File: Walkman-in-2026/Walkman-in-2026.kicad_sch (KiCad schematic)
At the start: 11 parts, among them J1 AudioJack3, J2 Micro_SD_Card, SW1 SW_Push, SW2 SW_Push, SW3 SW_Push, SW4 SW_SPST, U1 XIAO-ESP32-S3-DIP, U2 HS1602A-B, U3 PCM5102, U4 PCF8574P

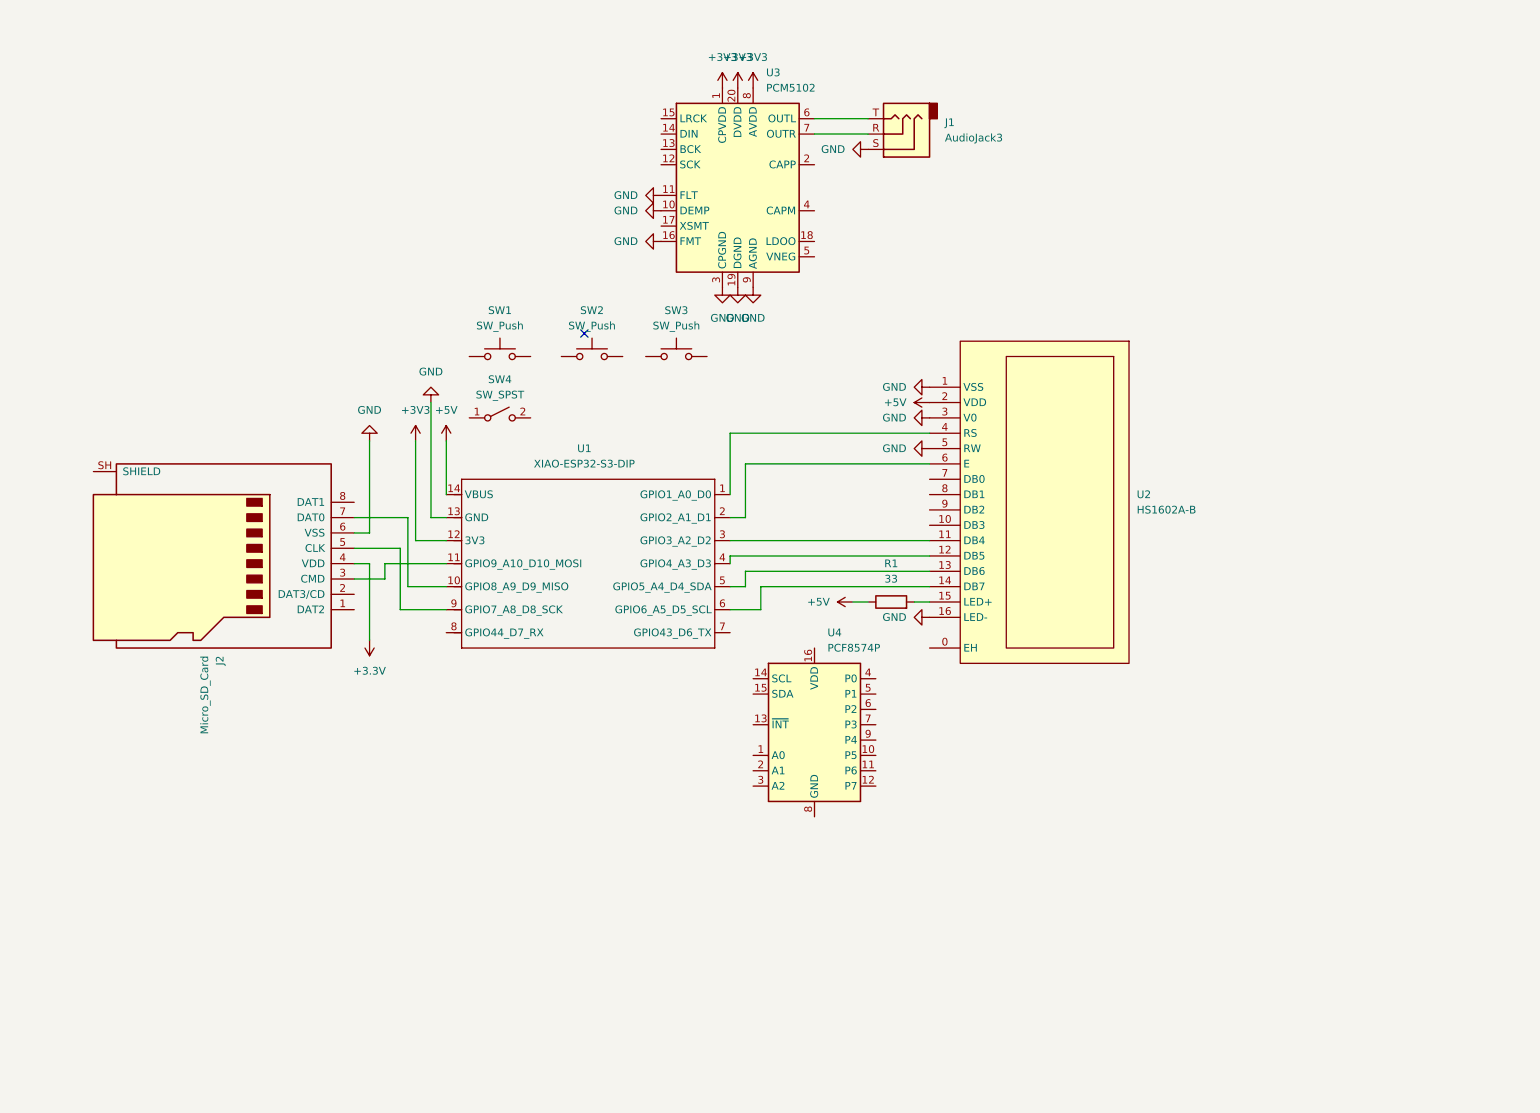
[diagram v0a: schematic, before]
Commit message: April 24 Session (Rerouting, Audio, Micro SD Card, and Setting Up Capacitors)
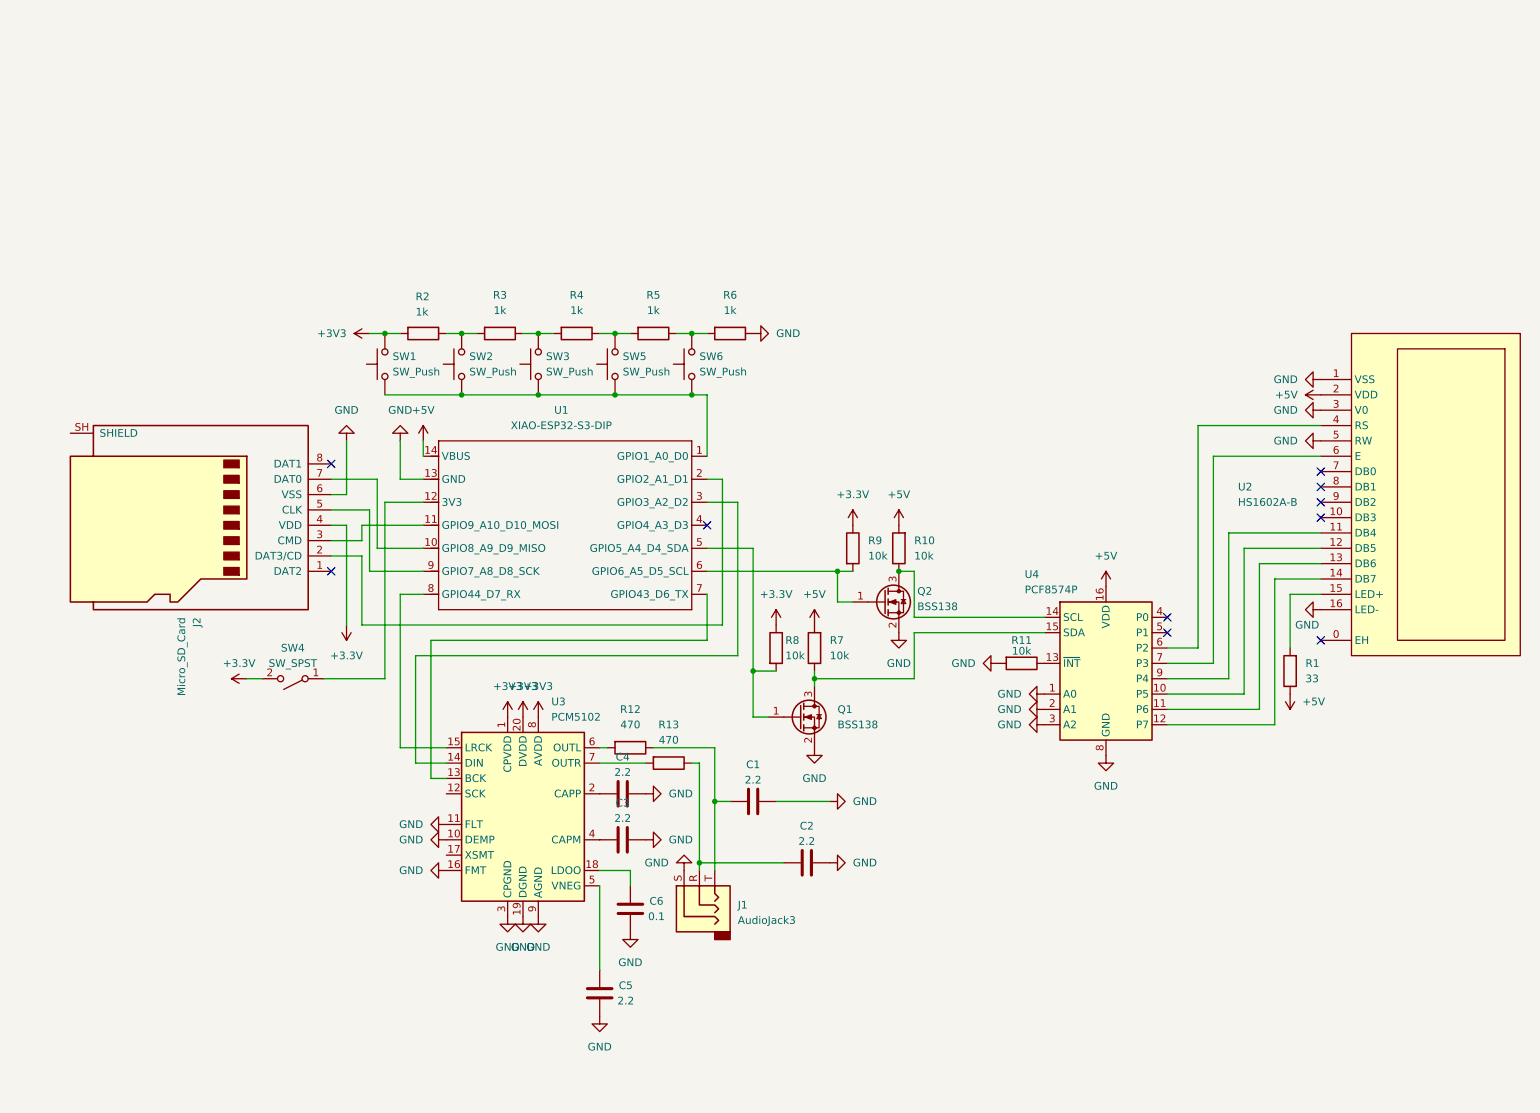
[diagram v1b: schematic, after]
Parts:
- added C1, C2, C3, C4, C5: 2.2, symbol Device:C
- added C6: 0.1, symbol Device:C
- added Q1, Q2: BSS138, Package_TO_SOT_SMD:SOT-23, symbol Transistor_FET:BSS138
- added R10, R11, R7, R8, R9: 10k, symbol Device:R
- added R12, R13: 470, symbol Device:R
- added R2, R3, R4, R5, R6: 1k, symbol Device:R
- added SW5, SW6: SW_Push, symbol Switch:SW_Push
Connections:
- net +3.3V: now also SW4.2 (B), R8.1, R9.1
- net +3V3: now also SW1.2, R2.2; no longer U1.12 (3V3)
- net +5V: now also U4.16 (VDD), R10.2, R7.2
- net GND: now also U4.1 (A0), U4.2 (A1), U4.3 (A2), U4.8 (GND), C1.2, C2.2, C3.2, C4.2, C5.2, C6.2, Q1.2 (S), Q2.2 (S), R11.2, R6.1
- net at U4.10 (P5): now also U2.12 (DB5)
- net at U4.11 (P6): now also U2.13 (DB6)
- net at U4.12 (P7): now also U2.14 (DB7)
- net at U4.13 (~{INT}): now also R11.1
- net at U4.14 (SCL): now also Q2.3 (D), R10.1
- net at U4.15 (SDA): now also Q1.3 (D), R7.1
- net at U4.6 (P2): now also U2.4 (RS)
- net at U4.7 (P3): now also U2.6 (E)
- net at U4.9 (P4): now also U2.11 (DB4)
- net at U3.13 (BCK): now also U1.7 (GPIO43_D6_TX)
- net at U3.14 (DIN): now also U1.3 (GPIO3_A2_D2)
- net at U3.15 (LRCK): now also U1.8 (GPIO44_D7_RX)
- net at U3.18 (LDOO): now also C6.1
- net at U3.2 (CAPP): now also C4.1
- net at U3.4 (CAPM): now also C3.1
- net at U3.5 (VNEG): now also C5.1
- net at U3.6 (OUTL): now also R12.2; no longer J1.T
- net at J1.R: now also C2.1, R13.1; no longer U3.7 (OUTR)
- net at J2.2 (DAT3/CD): now also U1.2 (GPIO2_A1_D1)
- net at SW4.1 (A): now also U1.12 (3V3)
- net at U1.1 (GPIO1_A0_D0): now also SW1.1, SW2.1, SW3.1, SW5.1, SW6.1; no longer U2.4 (RS)
- net at U1.4 (GPIO4_A3_D3): no longer U2.12 (DB5)
- net at U1.5 (GPIO5_A4_D4_SDA): now also Q1.1 (G), R8.2; no longer U2.13 (DB6)
- net at U1.6 (GPIO6_A5_D5_SCL): now also Q2.1 (G), R9.2; no longer U2.14 (DB7)
- net at SW3.2: now also R3.1, R4.2
- net at SW2.2: now also R2.1, R3.2
- new net: R5.1, R6.2, SW6.2
- new net: R4.1, R5.2, SW5.2
- new net: R13.2, U3.7 (OUTR)
- new net: C1.1, J1.T, R12.1
- no-connect marks 1 -> 10
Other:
- moved on the sheet: J1, J2, R1, SW1, SW2, SW3, SW4, U1, U2, U3, U4

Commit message: jazz fest working
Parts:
- added C10, C9: C, symbol Device:C
- added C7, C8: 0.1, symbol Device:C
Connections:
- net +3V3: now also U3.17 (XSMT), C10.1, C7.2, C8.2, C9.2
- net GND: now also U3.12 (SCK), C10.2, C7.1, C8.1, C9.1
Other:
- moved on the sheet: C1, C2, C3, C4, C5, C6, J1, R12, R13, U3

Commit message: moving on to the pcb editor
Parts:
- removed C4: 2.2, symbol Device:C
- C1, C2, C6, C7, C8: footprint (none) -> Capacitor_THT:C_Disc_D3.0mm_W1.6mm_P2.50mm
- C10: value C -> 10; footprint (none) -> Capacitor_THT:C_Radial_D5.0mm_H5.0mm_P2.00mm
- C3, C5: footprint (none) -> Capacitor_THT:C_Radial_D5.0mm_H5.0mm_P2.00mm
- C9: value C -> 0.1; footprint (none) -> Capacitor_THT:C_Radial_D5.0mm_H5.0mm_P2.00mm
- J1: footprint (none) -> Connector_Audio:Jack_3.5mm_CUI_SJ1-3513N_Horizontal
- J2: footprint (none) -> Connector_Card:microSD_HC_Molex_47219-2001
- R1, R10, R11, R12, R13, R2, R3, R4, R5, R6, R7, R8, R9: footprint (none) -> Resistor_THT:R_Axial_DIN0207_L6.3mm_D2.5mm_P7.62mm_Horizontal
- SW1, SW2, SW3, SW5, SW6: footprint (none) -> Button_Switch_THT:SW_PUSH_6mm
- SW4: footprint (none) -> Button_Switch_THT:SW_SPST_Omron_B3F-315x_Angled
- U1: footprint Seeed_Studio_XIAO_Series:XIAO-ESP32-S3-DIP -> More_XIAO_Series_Footprints:XIAO-ESP32-S3-DIP
- U2: footprint easyeda2kicad:LCD1602 -> EasyEDALibrary:LCD1602
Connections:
- net GND: now also C1.1, C2.1; no longer C1.2, C2.2, C3.2
- net at J1.R, R13.1: now also C2.2; no longer C2.1
- net at U3.2 (CAPP): now also C3.1
- net at U3.4 (CAPM): now also C3.2; no longer C3.1
- net at J1.T, R12.1: now also C1.2; no longer C1.1
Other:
- moved on the sheet: C1, C2, C3, C5, C6, C7, C8, J1, J2, Q1, Q2, R1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

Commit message: adding a fking stupid battery
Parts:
- added BT1: Battery, symbol Device:Battery
- added J3: Conn_01x02_Socket, Connector_Molex:Molex_KK-254_AE-6410-02A_1x02_P2.54mm_Vertical, symbol Connector:Conn_01x02_Socket
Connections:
- net +3.3V: now also U1.12 (3V3); no longer SW4.2 (B)
- net +5V: no longer U1.14 (VBUS)
- net GND: now also J3.2 (Pin_2)
- net at SW4.1 (A): now also U1.14 (VBUS); no longer U1.12 (3V3)
- new net: BT1.2 (-), SW4.2 (B)
- new net: BT1.1 (+), J3.1 (Pin_1)
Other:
- moved on the sheet: SW4

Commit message: larp
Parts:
- removed BT1: Battery, symbol Device:Battery
- removed C1, C2: 2.2, Capacitor_THT:C_Disc_D3.0mm_W1.6mm_P2.50mm, symbol Device:C
- removed C10: 10, Capacitor_THT:C_Radial_D5.0mm_H5.0mm_P2.00mm, symbol Device:C
- removed C3, C5: 2.2, Capacitor_THT:C_Radial_D5.0mm_H5.0mm_P2.00mm, symbol Device:C
- removed C6, C7, C8: 0.1, Capacitor_THT:C_Disc_D3.0mm_W1.6mm_P2.50mm, symbol Device:C
- removed C9: 0.1, Capacitor_THT:C_Radial_D5.0mm_H5.0mm_P2.00mm, symbol Device:C
- removed J1: AudioJack3, Connector_Audio:Jack_3.5mm_CUI_SJ1-3513N_Horizontal, symbol Connector_Audio:AudioJack3
- removed J3: Conn_01x02_Socket, Connector_Molex:Molex_KK-254_AE-6410-02A_1x02_P2.54mm_Vertical, symbol Connector:Conn_01x02_Socket
- removed R12, R13: 470, Resistor_THT:R_Axial_DIN0207_L6.3mm_D2.5mm_P7.62mm_Horizontal, symbol Device:R
- removed U3: PCM5102, Package_SO:TSSOP-20_4.4x6.5mm_P0.65mm, symbol Audio:PCM5102
- added J1: Conn_01x01_Pin, Connector_PinHeader_1.00mm:PinHeader_1x01_P1.00mm_Vertical, symbol Connector:Conn_01x01_Pin
- added JP1: Jumper_2_Bridged, TestPoint:TestPoint_2Pads_Pitch2.54mm_Drill0.8mm, symbol Jumper:Jumper_2_Bridged
- added U5: (no value), Connector_PinHeader_2.54mm:PinHeader_1x15_P2.54mm_Vertical, symbol Amazon _PCM:Amazon_and_AudioJack_PCM
- R2: value 1k -> 10k
- R4: value 1k -> 4.7k
- R5: value 1k -> 22k
- R6: value 1k -> 47k
- SW1, SW2, SW3, SW5, SW6: footprint Button_Switch_THT:SW_PUSH_6mm -> easyeda2kicad:SW-SMD_TC-S3601-3.5-260G-F0.6
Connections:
- net +3V3: now also U5.11 (A3V3), U5.9 (XSMT); no longer SW1.2
- net +5V: no longer R10.2, R7.2
- net GND: now also SW1.1, SW2.1, SW3.1, SW5.1, SW6.1, JP1.1 (A), U5.1 (SCK), U5.10 (FMT), U5.12 (AGND), U5.14 (AGND), U5.5 (GND), U5.7 (FLT), U5.8 (DEMP); no longer R6.1
- net GPIO1: now reaches R3.1, R4.2
- net GPIO1: now also R2.1, R5.1, R6.1, SW1.2, U1.1 (GPIO1_A0_D0); no longer SW3.2
- net at R3.2, SW2.2: no longer R2.1
- net at R6.2, SW6.2: no longer R5.1
- net at R5.2, SW5.2: no longer R4.1
- net at U1.7 (GPIO43_D6_TX): now also U5.2 (BCK)
- net at U1.3 (GPIO3_A2_D2): now also U5.3 (DIN)
- net at U1.8 (GPIO44_D7_RX): now also U5.4 (LCK)
- net at SW4.1 (A): now also J1.1 (Pin_1); no longer U1.14 (VBUS)
- net at SW4.2 (B): now also JP1.2 (B)
- new net: R4.1, SW3.2
- new net VBUS: R10.2, R7.2, U1.14 (VBUS), U5.6 (VIN)
- no-connect marks 10 -> 13
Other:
- moved on the sheet: R2, R3, R4, R5, R6, SW4

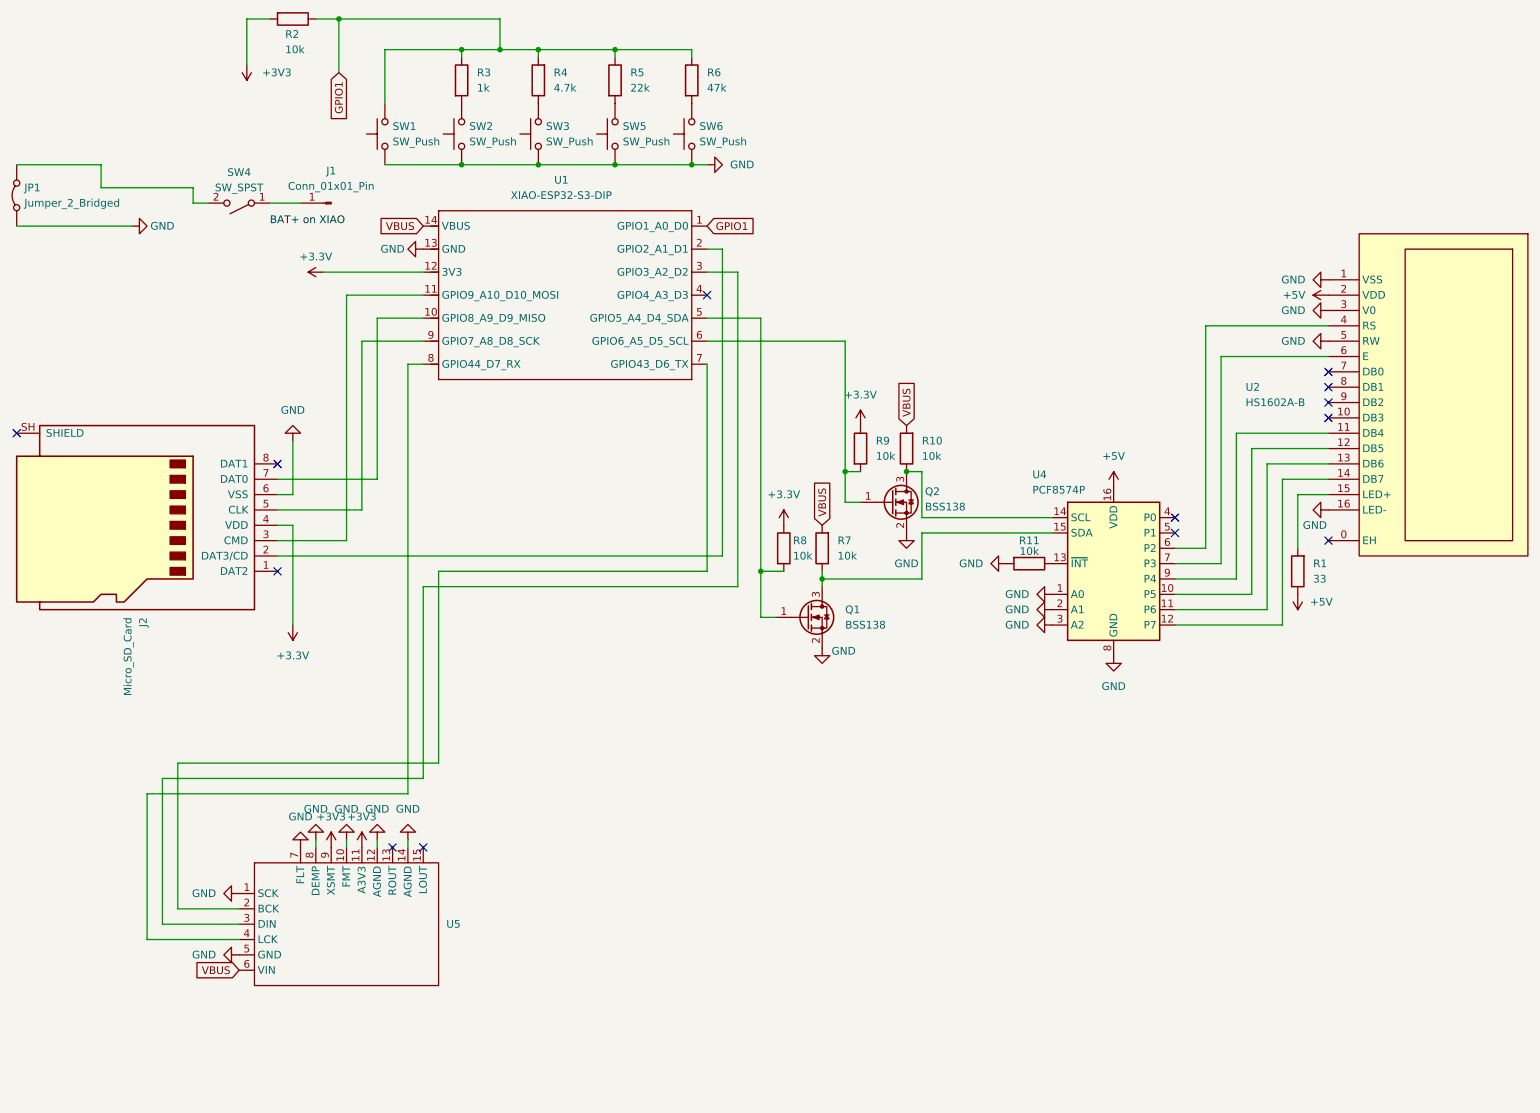
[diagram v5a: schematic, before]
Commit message: Adding custom footprints for lcd x pcf and pcm x audiojack
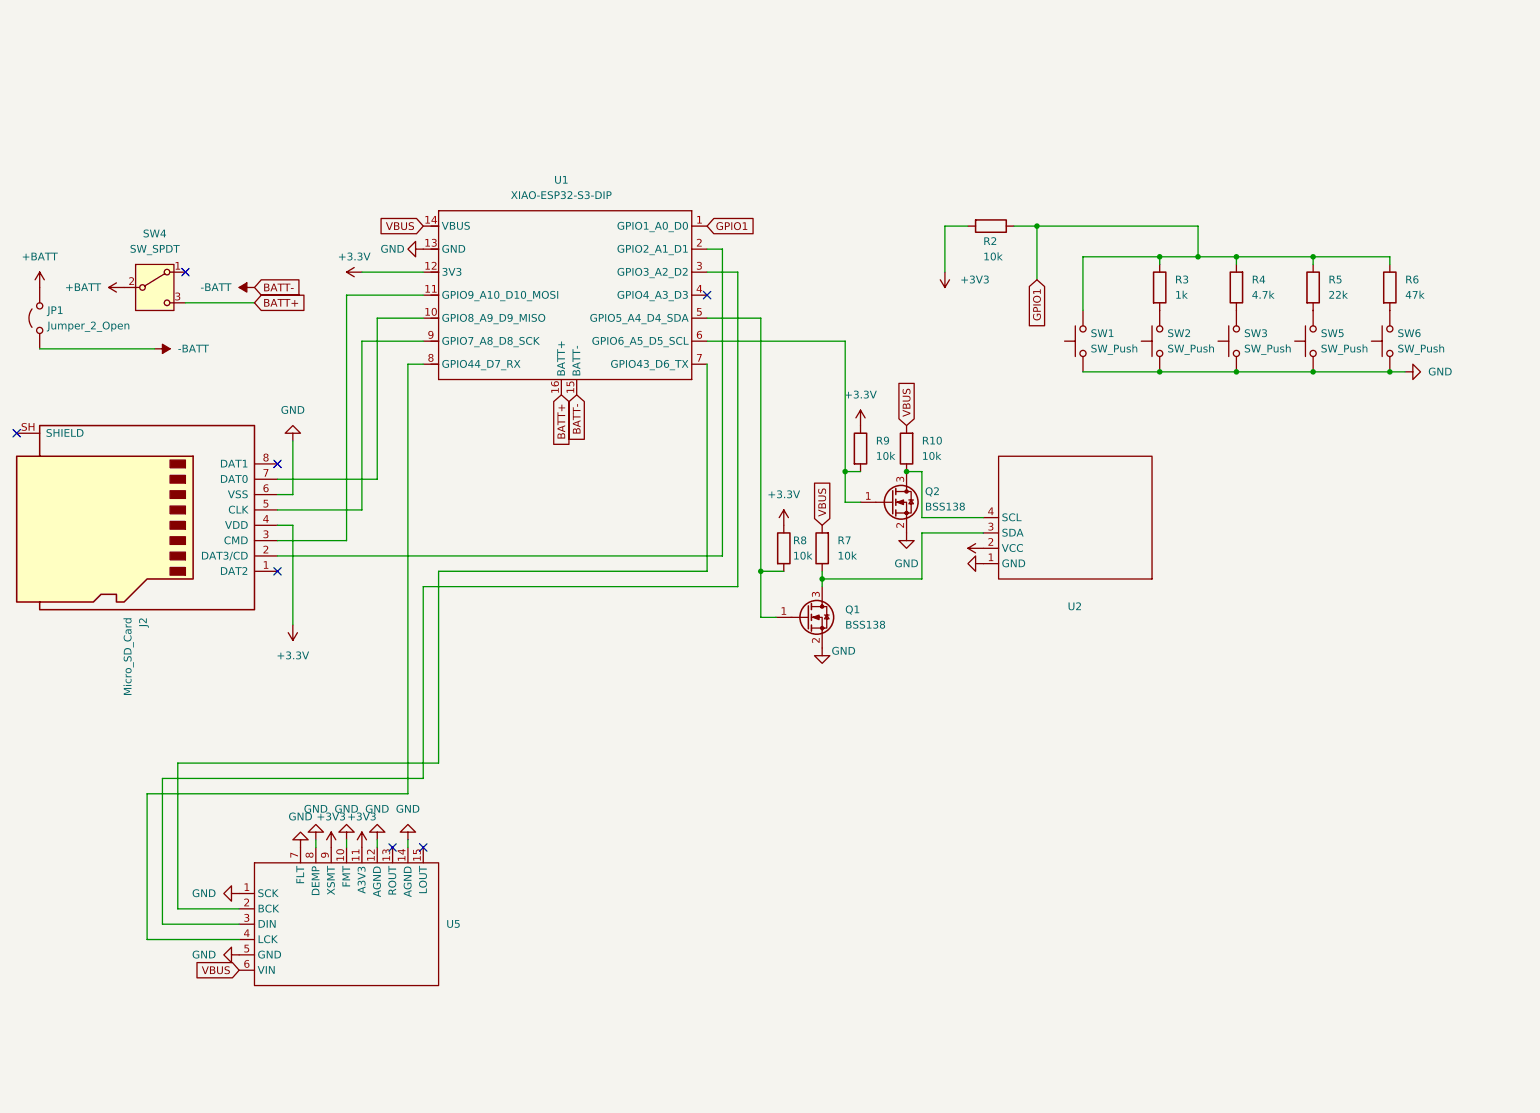
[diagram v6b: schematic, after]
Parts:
- removed J1: Conn_01x01_Pin, Connector_PinHeader_1.00mm:PinHeader_1x01_P1.00mm_Vertical, symbol Connector:Conn_01x01_Pin
- removed JP1: Jumper_2_Bridged, TestPoint:TestPoint_2Pads_Pitch2.54mm_Drill0.8mm, symbol Jumper:Jumper_2_Bridged
- removed R1: 33, Resistor_THT:R_Axial_DIN0207_L6.3mm_D2.5mm_P7.62mm_Horizontal, symbol Device:R
- removed R11: 10k, Resistor_THT:R_Axial_DIN0207_L6.3mm_D2.5mm_P7.62mm_Horizontal, symbol Device:R
- removed SW4: SW_SPST, Button_Switch_THT:SW_SPST_Omron_B3F-315x_Angled, symbol Switch:SW_SPST
- removed U2: HS1602A-B, EasyEDALibrary:LCD1602, symbol easyeda2kicad:HS1602A-B
- removed U4: PCF8574P, Package_DIP:DIP-16_W7.62mm, symbol Interface_Expansion:PCF8574P
- added JP1: Jumper_2_Open, TestPoint:TestPoint_2Pads_Pitch2.54mm_Drill0.8mm, symbol Jumper:Jumper_2_Open
- added SW4: SW_SPDT, Button_Switch_THT:SW_Slide_SPDT_Angled_CK_OS102011MA1Q, symbol Switch:SW_SPDT
- added U2: (no value), PCF x LCD combo:PCF8574 x LCD1602 combo, symbol PCF8574xLCD1602_combo:PCF8574xLCD1602_combo
- U5: footprint Connector_PinHeader_2.54mm:PinHeader_1x15_P2.54mm_Vertical -> Amazon_PCM:PCM x AudioJack Combo
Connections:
- net +5V: now also U2.2 (VCC)
- net GND: now also U2.1 (GND)
- net at Q2.3 (D), R10.1: now also U2.4 (SCL)
- net at Q1.3 (D), R7.1: now also U2.3 (SDA)
- new net +BATT: JP1.2 (B), SW4.2 (B)
- new net -BATT: JP1.1 (A), U1.15 (BATT-)
- new net BATT+: SW4.3 (C), U1.16 (BATT+)
- no-connect marks 13 -> 7
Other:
- moved on the sheet: R2, R3, R4, R5, R6, SW1, SW2, SW3, SW5, SW6
